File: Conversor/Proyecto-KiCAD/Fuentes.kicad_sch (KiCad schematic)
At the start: 15 parts

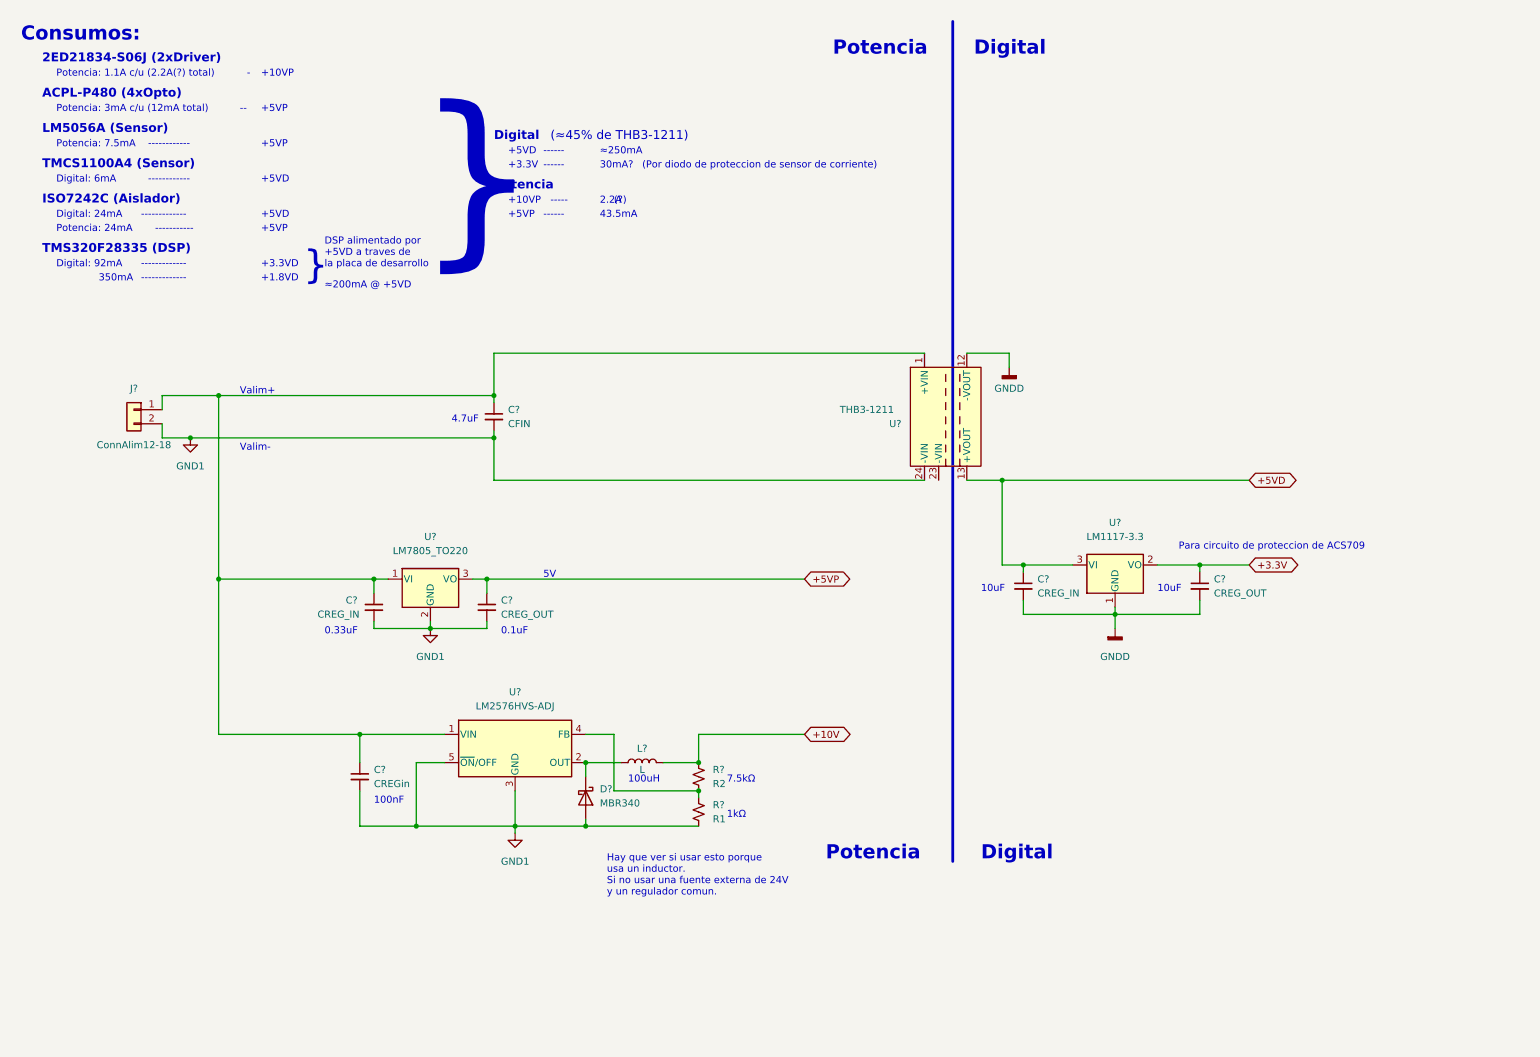
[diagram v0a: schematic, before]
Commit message: Empezar a arreglar los errores del ERC de KiCad
- Quedan muchos warnings pero un error de input power pin not driven
- Hay que hacer el esquematico general con alimentacion y preguntar
sobre el regulador de 10V
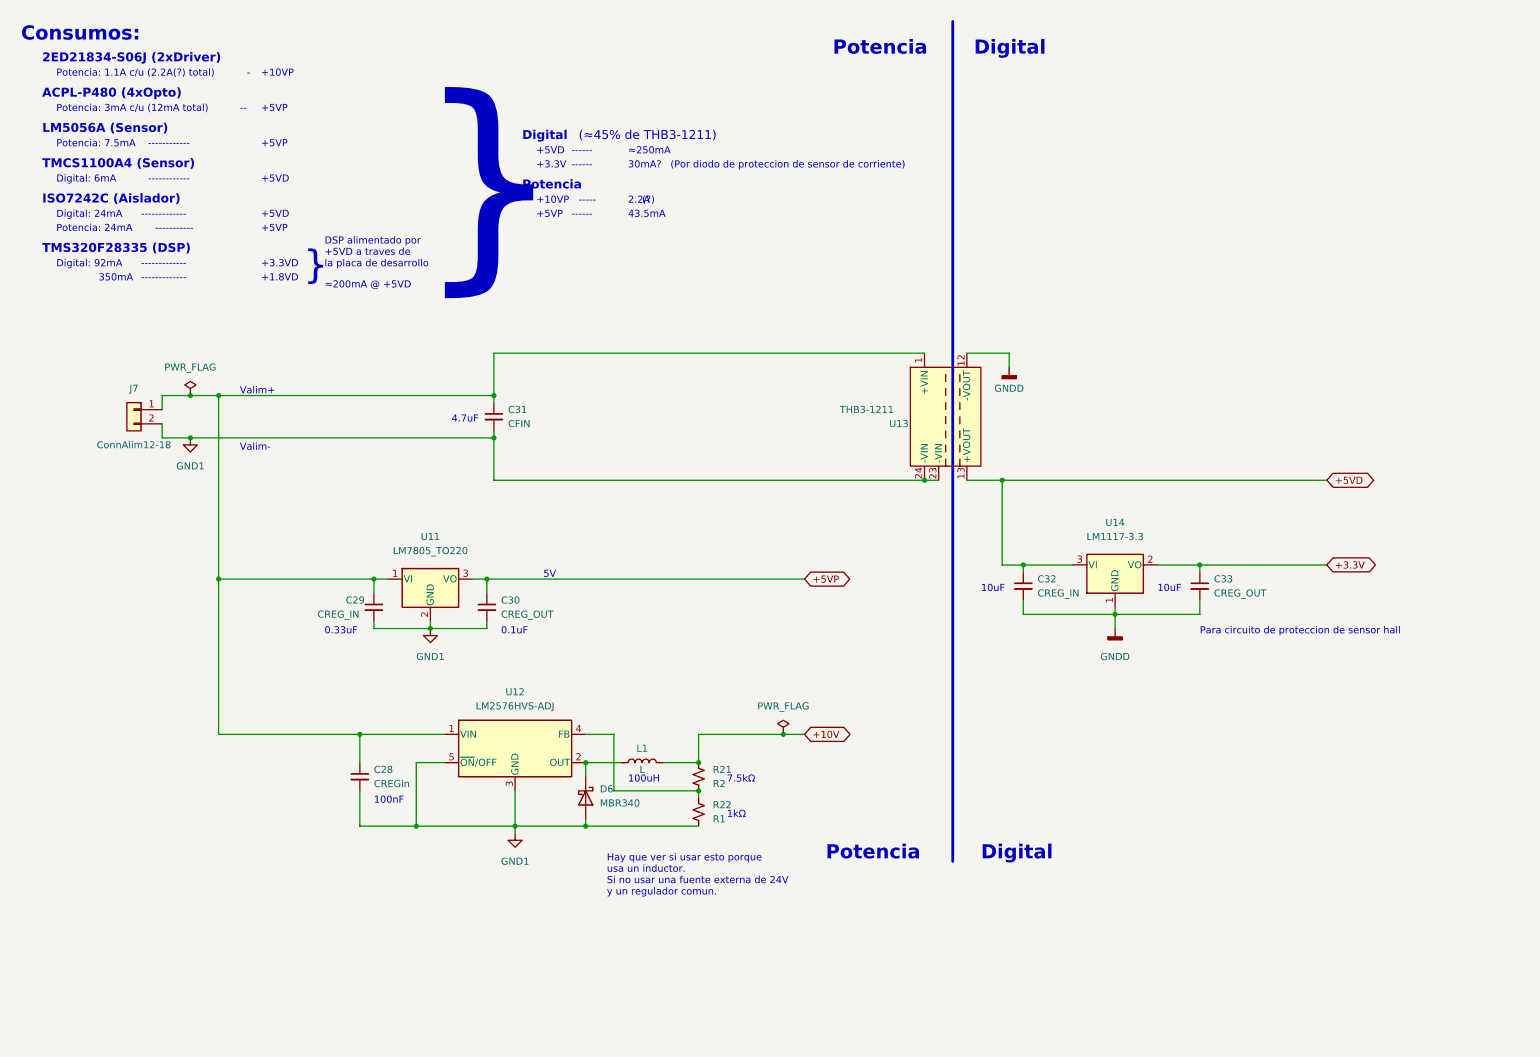
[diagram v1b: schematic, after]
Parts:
- gave numbers to parts that had none: 15
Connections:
- net GND1: now also U13.23 (-VIN)
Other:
- note added: "Para circuito de proteccion de sensor hall"
- note removed: "Para circuito de proteccion de ACS709"

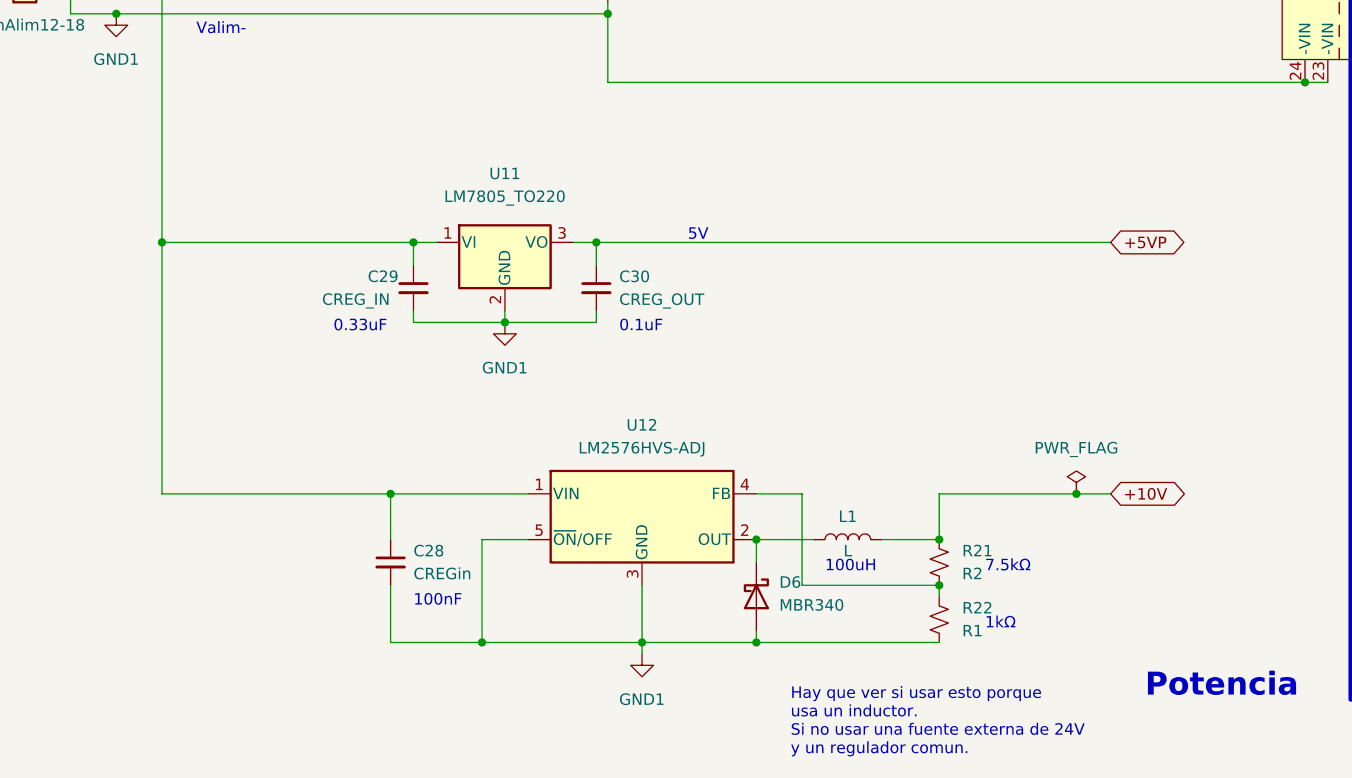
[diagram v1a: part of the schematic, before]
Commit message: Comenzar el diagrama mas detallado (en draw.io)
- Remover el regulador de 10V para los drivers, ahora se alimentan
directamente desde los 12-18V sin regulación
- Por hacer:
  - Falta agregar la alimentación y algunos labels en el    diagrama
  - Remover la hoja de datos del regulador de 10V
  - Pasar todos los componentes a subsheets como en la placa adaptadora,
de manera que quede como un diagrama de bloques
  - Una vez hecho eso, agregar el circuito de la placa adaptadora al
proyecto (tiene que ser todo una plaqueta)
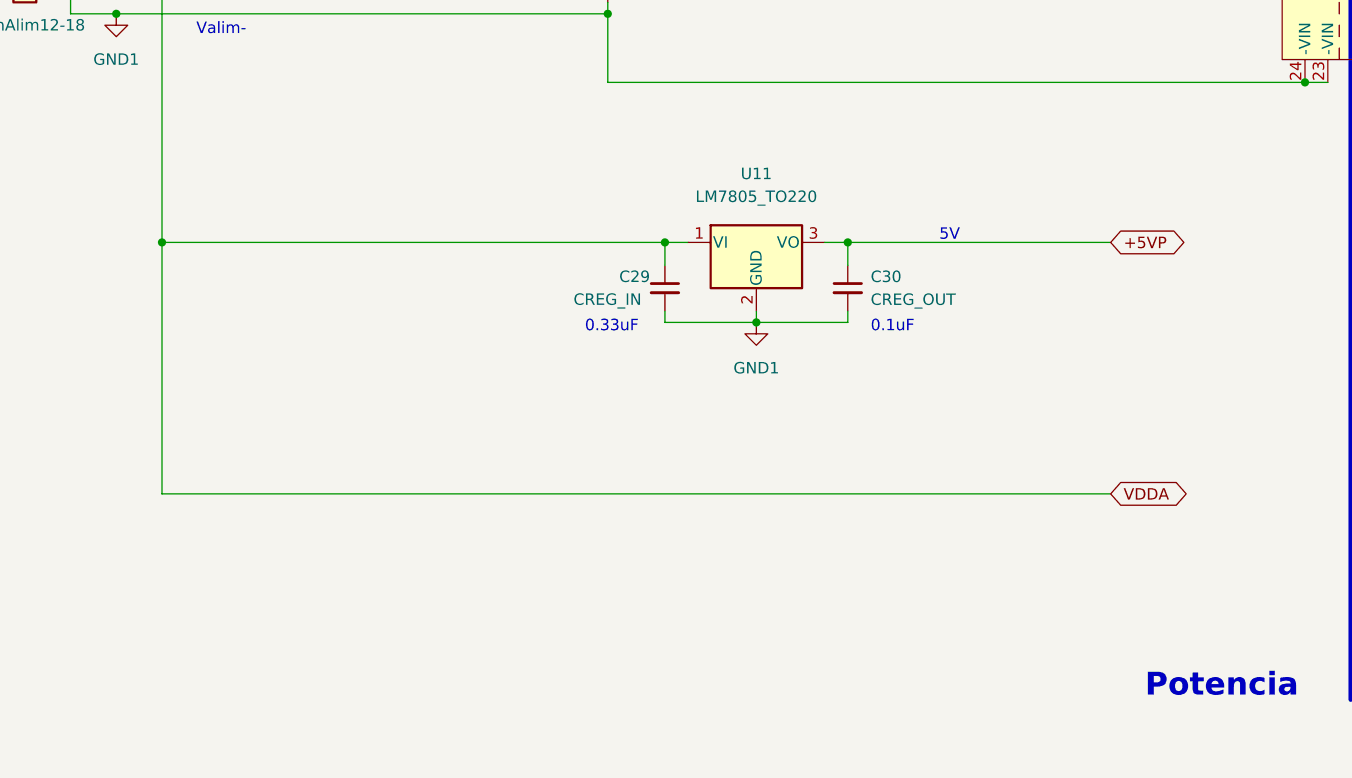
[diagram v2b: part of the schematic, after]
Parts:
- removed C28: CREGin, symbol Device:C_Small
- removed D6: MBR340, Diode_THT:D_DO-201AD_P15.24mm_Horizontal, symbol Diode:MBR340
- removed L1: L, symbol Device:L
- removed R21: R2, symbol Device:R_Small_US
- removed R22: R1, symbol Device:R_Small_US
- removed U12: LM2576HVS-ADJ, Package_TO_SOT_SMD:TO-263-5_TabPin3, symbol Regulator_Switching:LM2576HVS-ADJ
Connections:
- net VDDA: now reaches C29.1, C31.1, J7.1 (Pin_1), U11.1 (VI), U13.1 (+VIN)
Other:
- note removed: "100nF"
- note removed: "100uH"
- note removed: "1kΩ"
- note removed: "7.5kΩ"
- note removed: "Hay que ver si usar esto porque usa un inductor. Si no usar una fuente externa de 24V y un regulador comun."
- moved on the sheet: C29, C30, U11

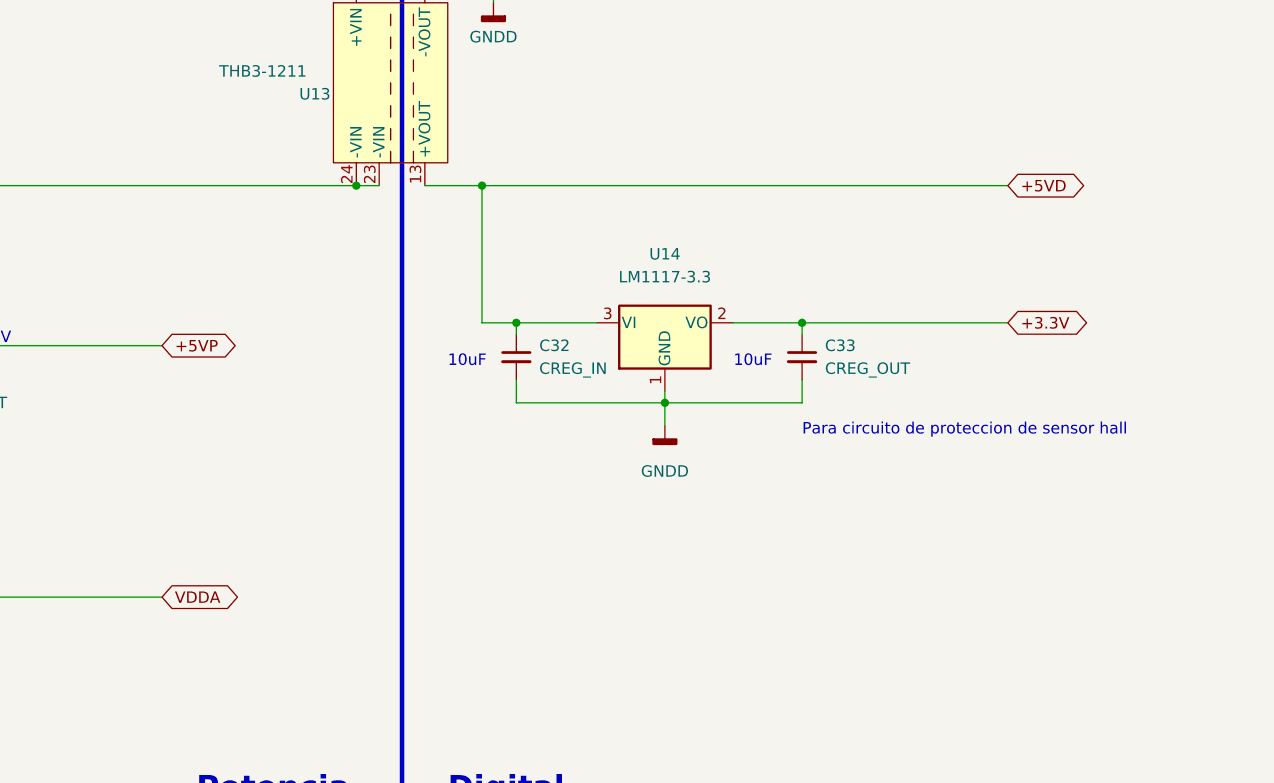
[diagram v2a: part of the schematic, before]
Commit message: Reestructurar el esquemático, con todo en heirarchical sheets
- Agregar la sheet de la placa adaptadora del DSP
Por hacer:
  - Completar la sheet del DSP con el proyecto de la placa adaptadora
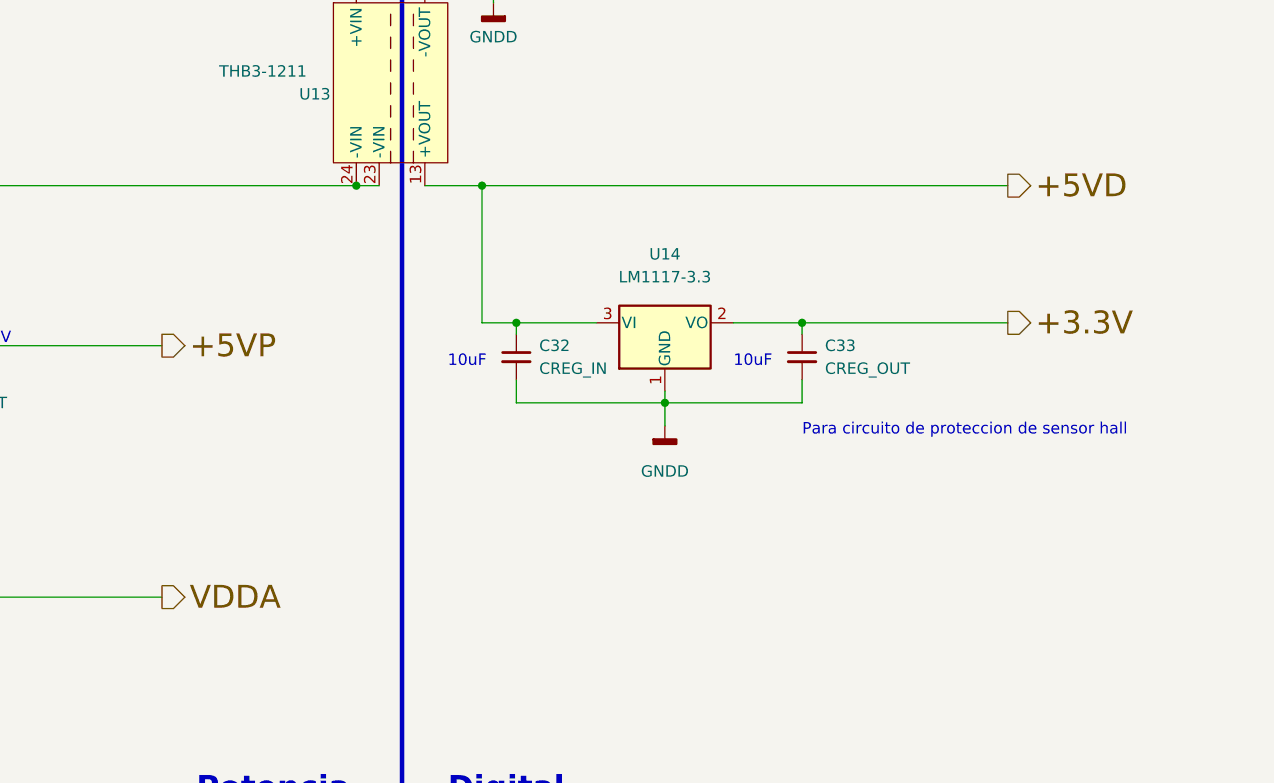
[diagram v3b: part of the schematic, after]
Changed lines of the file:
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@@
     (effects (font (size 1.27 1.27)) (justify left bottom))
   )
-  (global_label "+3.3V" (shape bidirectional) (at 247.65 110.49 0) (fields_autoplaced)
-    (effects (font (size 1.27 1.27)) (justify left))
-    (property "Intersheet References" "${INTERSHEET_REFS}" (id 0) (at 255.7479 110.4106 0)
-      (effects (font (size 1.27 1.27)) (justify left) hide)
-    )
+  (hierarchical_label "+5VP" (shape output) (at 153.67 113.03 0)
+    (effects (font (size 2.54 2.54)) (justify left))
   )
-  (global_label "+5VD" (shape bidirectional) (at 247.65 95.25 0) (fields_autoplaced)
-    (effects (font (size 1.27 1.27)) (justify left))
-    (property "Intersheet References" "${INTERSHEET_REFS}" (id 0) (at 255.2036 95.1706 0)
-      (effects (font (size 1.27 1.27)) (justify left) hide)
-    )
+  (hierarchical_label "VDDA" (shape output) (at 153.67 140.97 0)
+    (effects (font (size 2.54 2.54)) (justify left))
   )
-  (global_label "+5VP" (shape bidirectional) (at 153.67 113.03 0) (fields_autoplaced)
-    (effects (font (size 1.27 1.27)) (justify left))
-    (property "Intersheet References" "${INTERSHEET_REFS}" (id 0) (at 161.2236 112.9506 0)
-      (effects (font (size 1.27 1.27)) (justify left) hide)
-    )
+  (hierarchical_label "+3.3V" (shape output) (at 247.65 110.49 0)
+    (effects (font (size 2.54 2.54)) (justify left))
   )
-  (global_label "VDDA" (shape bidirectional) (at 153.67 140.97 0) (fields_autoplaced)
-    (effects (font (size 1.27 1.27)) (justify left))
-    (property "Intersheet References" "${INTERSHEET_REFS}" (id 0) (at 160.8002 140.8906 0)
-      (effects (font (size 1.27 1.27)) (justify left) hide)
-    )
+  (hierarchical_label "+5VD" (shape output) (at 247.65 95.25 0)
+    (effects (font (size 2.54 2.54)) (justify left))
   )
   (symbol (lib_id "Device:C_Small") (at 224.79 114.3 0) (unit 1)
